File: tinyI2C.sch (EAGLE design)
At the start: 30 parts, among them IC1 74ABT125BQ, IC2 TPS76318, U1 LPC824M201JHI33, X1 TSW-112-02-S-S, X2 TSW-106-02-S-S-RA, X3 TSW-112-02-S-S, X4 TSW-102-02-S-S

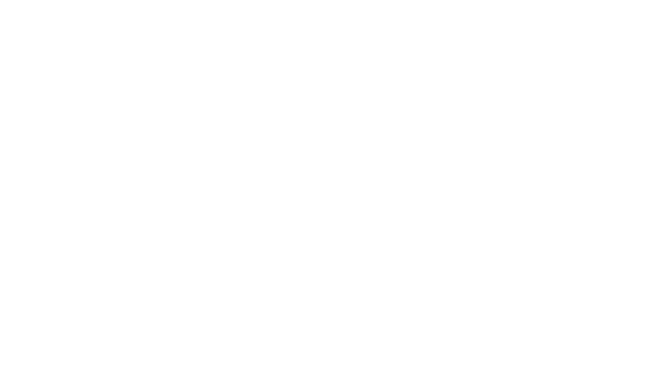
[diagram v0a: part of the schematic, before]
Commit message: added BOM list
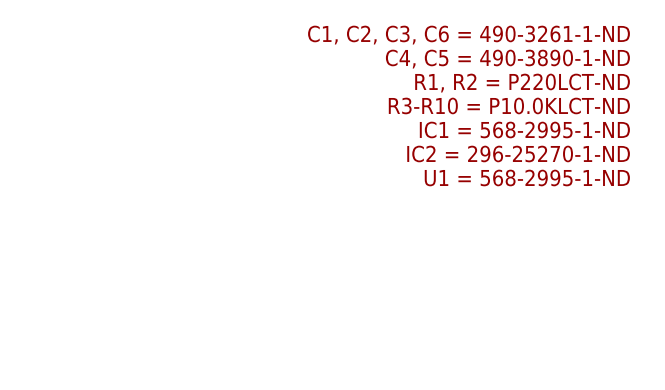
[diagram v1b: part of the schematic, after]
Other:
- note added: "C1, C2, C3, C6 = 490-3261-1-ND C4, C5 = 490-3890-1-ND R1, R2 = P220LCT-ND R3-R10 = P10.0KLCT-ND IC1 = 568-2995-1-ND IC2 = 296-25270-1-ND U1 = 568-2995-1-ND"
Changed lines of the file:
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@@
 <plain>
 <text x="231.14" y="40.64" size="1.778" layer="91">FIDUCIALS</text>
+<text x="254" y="172.72" size="1.778" layer="94" rot="R180">C1, C2, C3, C6 = 490-3261-1-ND
+C4, C5 = 490-3890-1-ND
+R1, R2 = P220LCT-ND
+R3-R10 = P10.0KLCT-ND
+IC1 = 568-2995-1-ND
+IC2 = 296-25270-1-ND
+U1 = 568-2995-1-ND</text>
 </plain>
 <instances>
@@
 </schematic>
 </drawing>
+<compatibility>
+<note version="6.3" minversion="6.2.2" severity="warning">
+Since Version 6.2.2 text objects can contain more than one line,
+which will not be processed correctly with this version.
+</note>
+</compatibility>
 </eagle>
